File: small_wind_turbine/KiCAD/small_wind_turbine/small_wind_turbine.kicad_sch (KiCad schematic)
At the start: 49 parts, among them K1 FINDER-36.11, SW1 SW_Push_SPDT, U2 UC2844A, U3 IRS10752LPBF, U4 Opamp_Quad, U5 AD8276, U6 AD8276, U7 MCP3021, U8 MCP4725xxx-xCH, U9 AZ1117-5.0

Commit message: after design review: calculate and add input capacitance
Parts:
- removed D7: D_Zener, symbol Device:D_Zener
- added C1: C, symbol Device:C
- added Cinput: 10u, symbol Device:C_Polarized
- added F1: 1.5A, symbol Device:Fuse
- added JP? (x2): Jumper_2_Bridged, symbol Jumper:Jumper_2_Bridged
- added Qbuck2: IRF6710S2, Package_DirectFET:DirectFET_S1, symbol Transistor_FET:IRF6710S2
- added R13: 30, symbol Device:R
- added R14: R, symbol Device:R
- added Rsh3: 50m, symbol Device:R
- gave numbers to parts that had none: 4
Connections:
- net GND: now also Cinput.2, JP?.1 (A), Rsh3.1; no longer A1.16 (GND), A1.4 (GND), Cbuck1.2, Ct1.2, Dbuck1.2 (A), Jbat1.2 (Pin_2), K1.A1, R1.2, R3.2, R5.2, R9.2, U2.5 (GND), U3.2 (COM), U4.4 (V+), U5.1 (REF), U5.4 (V-), U6.1 (REF), U6.4 (V-), U7.2 (VSS), U8.2 (VSS), U9.1 (GND)
- net RECTIFIER_VDD: now also Cinput.1
- net UC2844_GATE_OUTPUT: now also R13.1
- net at D1.1 (K), D3.1 (K), D5.1 (K): now also F1.1; no longer K1.11
- new net: JP?.1 (A), JP?.2 (B), Qbuck2.3 (S), Rsh3.2
- new net: F1.2, K1.11
- new net: Qbuck2.2 (G), R13.2
- new net GND1: A1.16 (GND), A1.4 (GND), Cbuck1.2, Ct1.2, Dbuck1.2 (A), JP?.2 (B), Jbat1.2 (Pin_2), K1.A1, Qbuck2.1 (D), R1.2, R3.2, R5.2, R9.2, U2.5 (GND), U3.2 (COM), U4.4 (V+), U5.1 (REF), U5.4 (V-), U6.1 (REF), U6.4 (V-), U7.2 (VSS), U8.2 (VSS), U9.1 (GND)
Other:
- note added: "Do not populate R13, Rsh3, or Qbuck2. Only used as alternate if high- side gate driver does not work"
- note added: "can this take 12V from the UC2844?"
- note removed: "3.3V For Protection"
- moved on the sheet: Cbuck1, Dbuck1, Jbat1, Lbuck1, Qbuck1, Rsh1, Rsh2

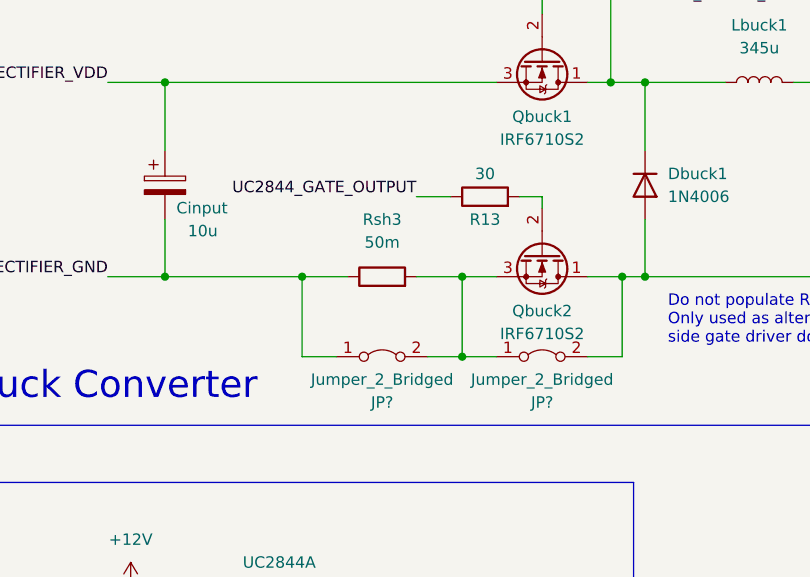
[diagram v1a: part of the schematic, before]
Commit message: remove extra low-side switch and shunt
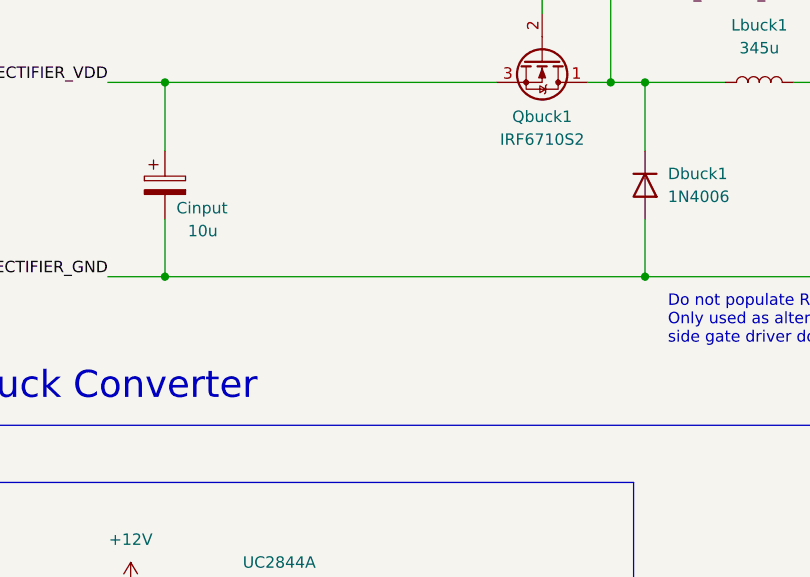
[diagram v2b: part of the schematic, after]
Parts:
- removed JP? (x2): Jumper_2_Bridged, symbol Jumper:Jumper_2_Bridged
- removed Qbuck2: IRF6710S2, Package_DirectFET:DirectFET_S1, symbol Transistor_FET:IRF6710S2
- removed R13: 30, symbol Device:R
- removed Rsh3: 50m, symbol Device:R
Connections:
- net GND1 is gone; now on net GND: A1.16 (GND), A1.4 (GND), Cbuck1.2, Ct1.2, Dbuck1.2 (A), Jbat1.2 (Pin_2), K1.A1, R1.2, R3.2, R5.2, R9.2, U2.5 (GND), U3.2 (COM), U4.4 (V+), U5.1 (REF), U5.4 (V-), U6.1 (REF), U6.4 (V-), U7.2 (VSS), U8.2 (VSS), U9.1 (GND)
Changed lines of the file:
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@@
   (junction (at 223.52 168.91) (diameter 0) (color 0 0 0 0)
   )
-  (junction (at 73.66 123.19) (diameter 0) (color 0 0 0 0)
-  )
   (junction (at 67.31 246.38) (diameter 0) (color 0 0 0 0)
   )
@@
   (junction (at 256.54 171.45) (diameter 0) (color 0 0 0 0)
   )
-  (junction (at 73.66 132.08) (diameter 0) (color 0 0 0 0)
-  )
   (junction (at 40.64 101.6) (diameter 0) (color 0 0 0 0)
   )
@@
   (junction (at 73.025 53.34) (diameter 0) (color 0 0 0 0)
   )
-  (junction (at 55.88 123.19) (diameter 0) (color 0 0 0 0)
-  )
   (junction (at 128.27 231.14) (diameter 0) (color 0 0 0 0)
   )
   (junction (at 90.17 101.6) (diameter 0) (color 0 0 0 0)
-  )
-  (junction (at 91.44 123.19) (diameter 0) (color 0 0 0 0)
   )
   (no_connect (at 350.52 69.85))
@@
     (stroke (width 0) (type default) (color 0 0 0 0))
   )
-  (wire (pts (xy 40.64 123.19) (xy 55.88 123.19))
+  (wire (pts (xy 40.64 123.19) (xy 93.98 123.19))
     (stroke (width 0) (type default) (color 0 0 0 0))
   )
@@
     (stroke (width 0) (type default) (color 0 0 0 0))
   )
-  (wire (pts (xy 59.69 132.08) (xy 55.88 132.08))
-    (stroke (width 0) (type default) (color 0 0 0 0))
-  )
   (wire (pts (xy 370.84 50.8) (xy 370.84 48.26))
     (stroke (width 0) (type default) (color 0 0 0 0))
@@
     (stroke (width 0) (type default) (color 0 0 0 0))
   )
-  (wire (pts (xy 68.58 123.19) (xy 73.66 123.19))
-    (stroke (width 0) (type default) (color 0 0 0 0))
-  )
   (wire (pts (xy 172.72 163.83) (xy 167.64 163.83))
     (stroke (width 0) (type default) (color 0 0 0 0))
@@
     (stroke (width 0) (type default) (color 0 0 0 0))
   )
-  (wire (pts (xy 87.63 123.19) (xy 91.44 123.19))
-    (stroke (width 0) (type default) (color 0 0 0 0))
-  )
   (wire (pts (xy 363.22 50.8) (xy 363.22 48.26))
     (stroke (width 0) (type default) (color 0 0 0 0))
@@
     (stroke (width 0) (type default) (color 0 0 0 0))
   )
-  (wire (pts (xy 91.44 123.19) (xy 93.98 123.19))
-    (stroke (width 0) (type default) (color 0 0 0 0))
-  )
   (wire (pts (xy 267.97 53.34) (xy 241.3 53.34))
     (stroke (width 0) (type default) (color 0 0 0 0))
@@
     (stroke (width 0) (type default) (color 0 0 0 0))
   )
-  (wire (pts (xy 55.88 132.08) (xy 55.88 123.19))
-    (stroke (width 0) (type default) (color 0 0 0 0))
-  )
   (wire (pts (xy 137.16 101.6) (xy 140.97 101.6))
     (stroke (width 0) (type default) (color 0 0 0 0))
   )
-  (wire (pts (xy 55.88 123.19) (xy 60.96 123.19))
-    (stroke (width 0) (type default) (color 0 0 0 0))
-  )
   (wire (pts (xy 40.64 101.6) (xy 40.64 109.22))
     (stroke (width 0) (type default) (color 0 0 0 0))
@@
     (stroke (width 0) (type default) (color 0 0 0 0))
   )
-  (wire (pts (xy 80.01 114.3) (xy 82.55 114.3))
-    (stroke (width 0) (type default) (color 0 0 0 0))
-  )
   (wire (pts (xy 377.19 186.69) (xy 368.3 186.69))
     (stroke (width 0) (type default) (color 0 0 0 0))
@@
     (stroke (width 0) (type default) (color 0 0 0 0))
   )
-  (wire (pts (xy 73.66 132.08) (xy 77.47 132.08))
-    (stroke (width 0) (type default) (color 0 0 0 0))
-  )
   (wire (pts (xy 363.22 115.57) (xy 363.22 119.38))
     (stroke (width 0) (type default) (color 0 0 0 0))
@@
     (stroke (width 0) (type default) (color 0 0 0 0))
   )
-  (wire (pts (xy 82.55 114.3) (xy 82.55 115.57))
-    (stroke (width 0) (type default) (color 0 0 0 0))
-  )
   (wire (pts (xy 267.97 45.72) (xy 267.97 53.34))
     (stroke (width 0) (type default) (color 0 0 0 0))
@@
     (stroke (width 0) (type default) (color 0 0 0 0))
   )
-  (wire (pts (xy 68.58 114.3) (xy 72.39 114.3))
-    (stroke (width 0) (type default) (color 0 0 0 0))
-  )
-  (wire (pts (xy 73.66 132.08) (xy 73.66 123.19))
-    (stroke (width 0) (type default) (color 0 0 0 0))
-  )
   (wire (pts (xy 322.58 186.69) (xy 328.93 186.69))
     (stroke (width 0) (type default) (color 0 0 0 0))
@@
     (stroke (width 0) (type default) (color 0 0 0 0))
   )
-  (wire (pts (xy 91.44 123.19) (xy 91.44 132.08))
-    (stroke (width 0) (type default) (color 0 0 0 0))
-  )
   (wire (pts (xy 251.46 171.45) (xy 256.54 171.45))
     (stroke (width 0) (type default) (color 0 0 0 0))
@@
     (stroke (width 0) (type default) (color 0 0 0 0))
   )
-  (wire (pts (xy 73.66 123.19) (xy 77.47 123.19))
-    (stroke (width 0) (type default) (color 0 0 0 0))
-  )
   (wire (pts (xy 232.41 182.88) (xy 256.54 182.88))
     (stroke (width 0) (type default) (color 0 0 0 0))
   )
-  (wire (pts (xy 91.44 132.08) (xy 87.63 132.08))
-    (stroke (width 0) (type default) (color 0 0 0 0))
-  )
   (wire (pts (xy 328.93 179.07) (xy 328.93 186.69))
     (stroke (width 0) (type default) (color 0 0 0 0))
@@
   )
   (polyline (pts (xy 403.86 134.62) (xy 403.86 16.51))
-    (stroke (width 0) (type default) (color 0 0 0 0))
-  )
-  (wire (pts (xy 69.85 132.08) (xy 73.66 132.08))
     (stroke (width 0) (type default) (color 0 0 0 0))
   )
@@
   (label "OUTPUT_ISENSE_DOWNSTREAM" (at 157.48 92.71 0)
     (effects (font (size 1.27 1.27)) (justify left bottom))
-  )
-  (label "UC2844_GATE_OUTPUT" (at 68.58 114.3 180)
-    (effects (font (size 1.27 1.27)) (justify right bottom))
   )
   (label "BATTERY_POSITIVE" (at 177.8 101.6 0)
@@
     )
     (property "Datasheet" "~" (id 3) (at 359.41 196.85 0)
-      (effects (font (size 1.27 1.27)) hide)
-    )
-    (pin "1")
-    (pin "2")
-  )
-  (symbol (lib_id "Device:R") (at 64.77 123.19 90) (unit 1)
-    (in_bom yes) (on_board yes) (fields_autoplaced)
-    (property "Reference" "Rsh3" (id 0) (at 64.77 116.84 90))
-    (property "Value" "50m" (id 1) (at 64.77 119.38 90))
-    (property "Footprint" "" (id 2) (at 64.77 124.968 90)
-      (effects (font (size 1.27 1.27)) hide)
-    )
-    (property "Datasheet" "~" (id 3) (at 64.77 123.19 0)
       (effects (font (size 1.27 1.27)) hide)
     )
@@
     )
     (property "Datasheet" "http://www.vishay.com/docs/88516/1n5400.pdf" (id 3) (at 50.165 31.75 0)
-      (effects (font (size 1.27 1.27)) hide)
-    )
-    (pin "1")
-    (pin "2")
-  )
-  (symbol (lib_id "Jumper:Jumper_2_Bridged") (at 64.77 132.08 0) (unit 1)
-    (in_bom yes) (on_board yes)
-    (property "Reference" "JP?" (id 0) (at 64.77 137.16 0))
-    (property "Value" "Jumper_2_Bridged" (id 1) (at 64.77 134.62 0))
-    (property "Footprint" "" (id 2) (at 64.77 132.08 0)
-      (effects (font (size 1.27 1.27)) hide)
-    )
-    (property "Datasheet" "~" (id 3) (at 64.77 132.08 0)
       (effects (font (size 1.27 1.27)) hide)
     )
@@
     )
     (property "Datasheet" "~" (id 3) (at 342.9 196.85 0)
-      (effects (font (size 1.27 1.27)) hide)
-    )
-    (pin "1")
-    (pin "2")
-  )
-  (symbol (lib_id "Jumper:Jumper_2_Bridged") (at 82.55 132.08 0) (unit 1)
-    (in_bom yes) (on_board yes)
-    (property "Reference" "JP?" (id 0) (at 82.55 137.16 0))
-    (property "Value" "Jumper_2_Bridged" (id 1) (at 82.55 134.62 0))
-    (property "Footprint" "" (id 2) (at 82.55 132.08 0)
-      (effects (font (size 1.27 1.27)) hide)
-    )
-    (property "Datasheet" "~" (id 3) (at 82.55 132.08 0)
       (effects (font (size 1.27 1.27)) hide)
     )
@@
     (pin "1")
     (pin "2")
-  )
-  (symbol (lib_id "Transistor_FET:IRF6710S2") (at 82.55 120.65 270) (unit 1)
-    (in_bom yes) (on_board yes)
-    (property "Reference" "Qbuck2" (id 0) (at 82.55 127 90))
-    (property "Value" "IRF6710S2" (id 1) (at 82.55 129.54 90))
-    (property "Footprint" "Package_DirectFET:DirectFET_S1" (id 2) (at 82.55 120.65 0)
-      (effects (font (size 1.27 1.27) italic) hide)
-    )
-    (property "Datasheet" "https://www.infineon.com/dgdl/irf6710s2pbf.pdf?fileId=5546d462533600a4015355ece3db1a78" (id 3) (at 82.55 120.65 0)
-      (effects (font (size 1.27 1.27)) (justify left) hide)
-    )
-    (pin "1")
-    (pin "2")
-    (pin "3")
   )
   (symbol (lib_id "MCU_Module:Adafruit_Feather_M0_Adalogger") (at 363.22 82.55 0) (unit 1)
@@
     (pin "2")
   )
-  (symbol (lib_id "Device:R") (at 76.2 114.3 90) (unit 1)
-    (in_bom yes) (on_board yes)
-    (property "Reference" "R13" (id 0) (at 76.2 116.84 90))
-    (property "Value" "30" (id 1) (at 76.2 111.76 90))
-    (property "Footprint" "" (id 2) (at 76.2 116.078 90)
-      (effects (font (size 1.27 1.27)) hide)
-    )
-    (property "Datasheet" "~" (id 3) (at 76.2 114.3 0)
-      (effects (font (size 1.27 1.27)) hide)
-    )
-    (pin "1")
-    (pin "2")
-  )
   (symbol (lib_id "Device:R") (at 232.41 52.07 0) (unit 1)
     (in_bom yes) (on_board yes) (fields_autoplaced)
@@
       (reference "J2") (unit 1) (value "Conn_01x03_Male") (footprint "")
     )
-    (path "/21ae93f8-e8b3-46c7-9487-67b730704ffc"
-      (reference "JP?") (unit 1) (value "Jumper_2_Bridged") (footprint "")
-    )
-    (path "/3e2aea01-38ce-48ce-bf99-7656b70688aa"
-      (reference "JP?") (unit 1) (value "Jumper_2_Bridged") (footprint "")
-    )
     (path "/c346af4d-70e6-4239-ae69-840d06e1dca9"
       (reference "Jbat1") (unit 1) (value "Screw_Terminal_01x02") (footprint "")
@@
       (reference "Qbuck1") (unit 1) (value "IRF6710S2") (footprint "Package_DirectFET:DirectFET_S1")
     )
-    (path "/759998f2-ff86-422e-8ef7-c459ade9d521"
-      (reference "Qbuck2") (unit 1) (value "IRF6710S2") (footprint "Package_DirectFET:DirectFET_S1")
-    )
     (path "/928f9c53-7ad5-4dd7-8760-30969de9b03b"
       (reference "R1") (unit 1) (value "4.7k") (footprint "")
@@
       (reference "R12") (unit 1) (value "10") (footprint "")
     )
-    (path "/c3f14a14-b069-4ebc-bddf-9e873e12353b"
-      (reference "R13") (unit 1) (value "30") (footprint "")
-    )
     (path "/1fa2c91c-e88f-4872-8935-c1d7a8d8c3b1"
       (reference "R14") (unit 1) (value "R") (footprint "")
@@
       (reference "Rsh2") (unit 1) (value "50m") (footprint "")
     )
-    (path "/08afaf65-63eb-43a0-9fba-405598d4434c"
-      (reference "Rsh3") (unit 1) (value "50m") (footprint "")
-    )
     (path "/7da34064-fe09-4834-a1fe-c425bf57d2d4"

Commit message: substitute different diff amp with 20V/V gain
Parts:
- removed R2: 9k, symbol Device:R
- removed R3: 1k, symbol Device:R
- removed U5, U6: AD8276, symbol Amplifier_Difference:AD8276
- added U? (x2): INA240A1D, Package_SO:SOIC-8_3.9x4.9mm_P1.27mm, symbol Amplifier_Current:INA240A1D
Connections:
- net +12V: now also U?.1 (-), U?.8 (+)
- net +5V: now also U?.6 (V+), U?.6 (V+)
- net BATTERY_POSITIVE: now also U?.1 (-)
- net GND: now also U?.2 (GND), U?.2 (GND), U?.3 (REF2), U?.3 (REF2), U?.4 (GND), U?.4 (GND), U?.7 (REF1), U?.7 (REF1)
- net INPUT_ISENSE_UPSTREAM: now also U?.8 (+)
- net UC2844_ISENSE: now also U?.5
- net at U4.1: now also R6.2, U4.2 (-); no longer U4.5 (+)
- net at U4.3 (+): now also U?.5
- now unconnected: U4.6 (-), U4.7
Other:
- moved on the sheet: Cbs1, Cc1, Cc2, Dbs1, J1, R12, R6, R7, R8, R9, Rc1, Rf1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
